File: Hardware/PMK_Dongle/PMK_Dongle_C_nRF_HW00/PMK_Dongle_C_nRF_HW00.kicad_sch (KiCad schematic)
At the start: 2 parts, among them J1 USB4151-GF-C, U1 NRF52840-CKAA-F-R7

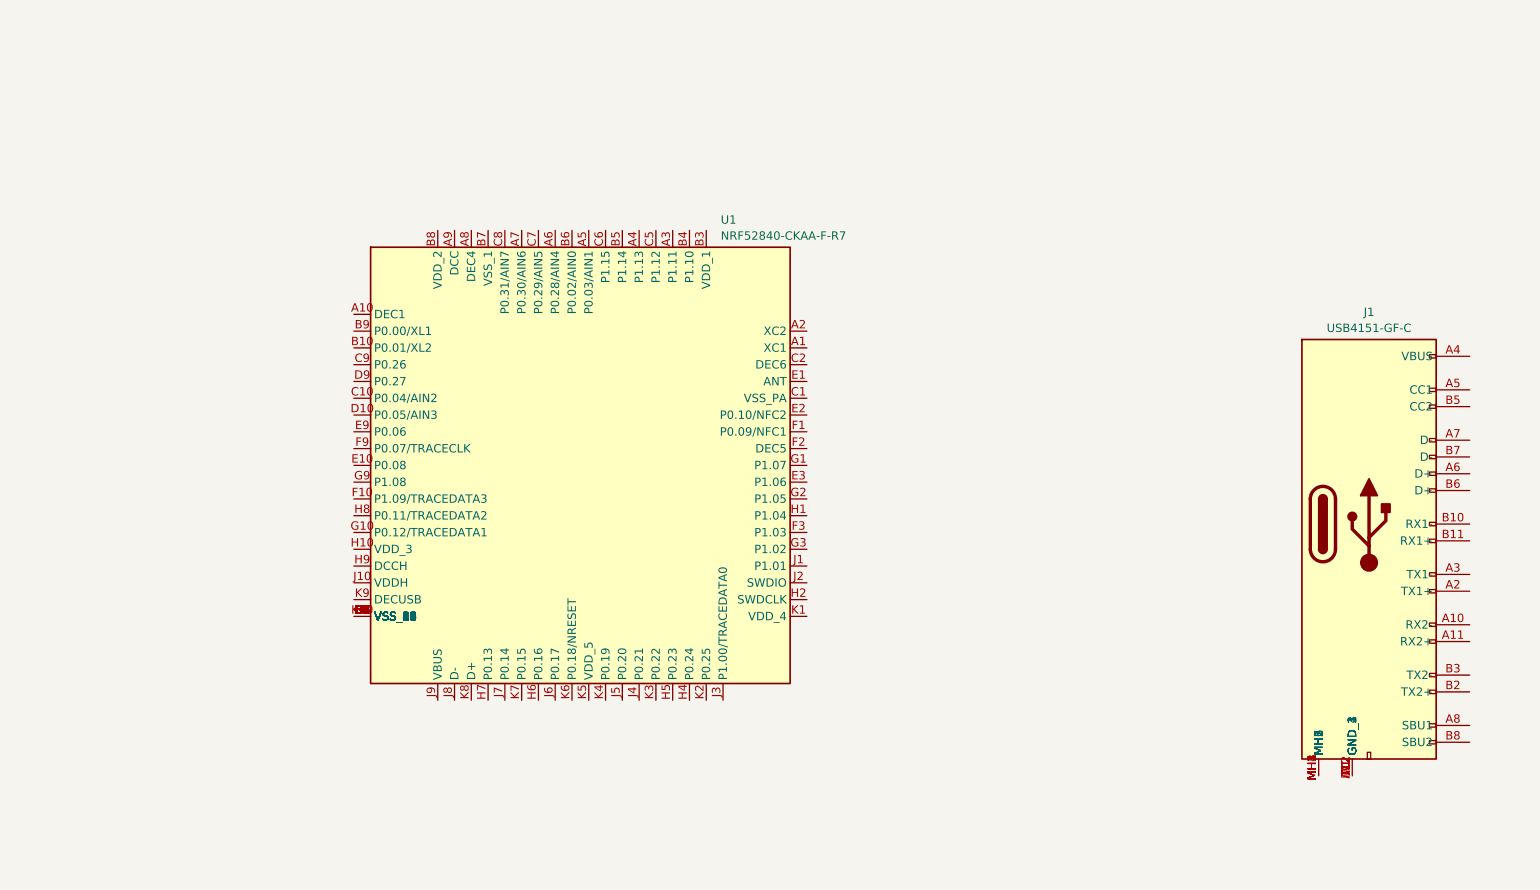
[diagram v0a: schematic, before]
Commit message: started routing PMK_Dongle_C_NRF_00
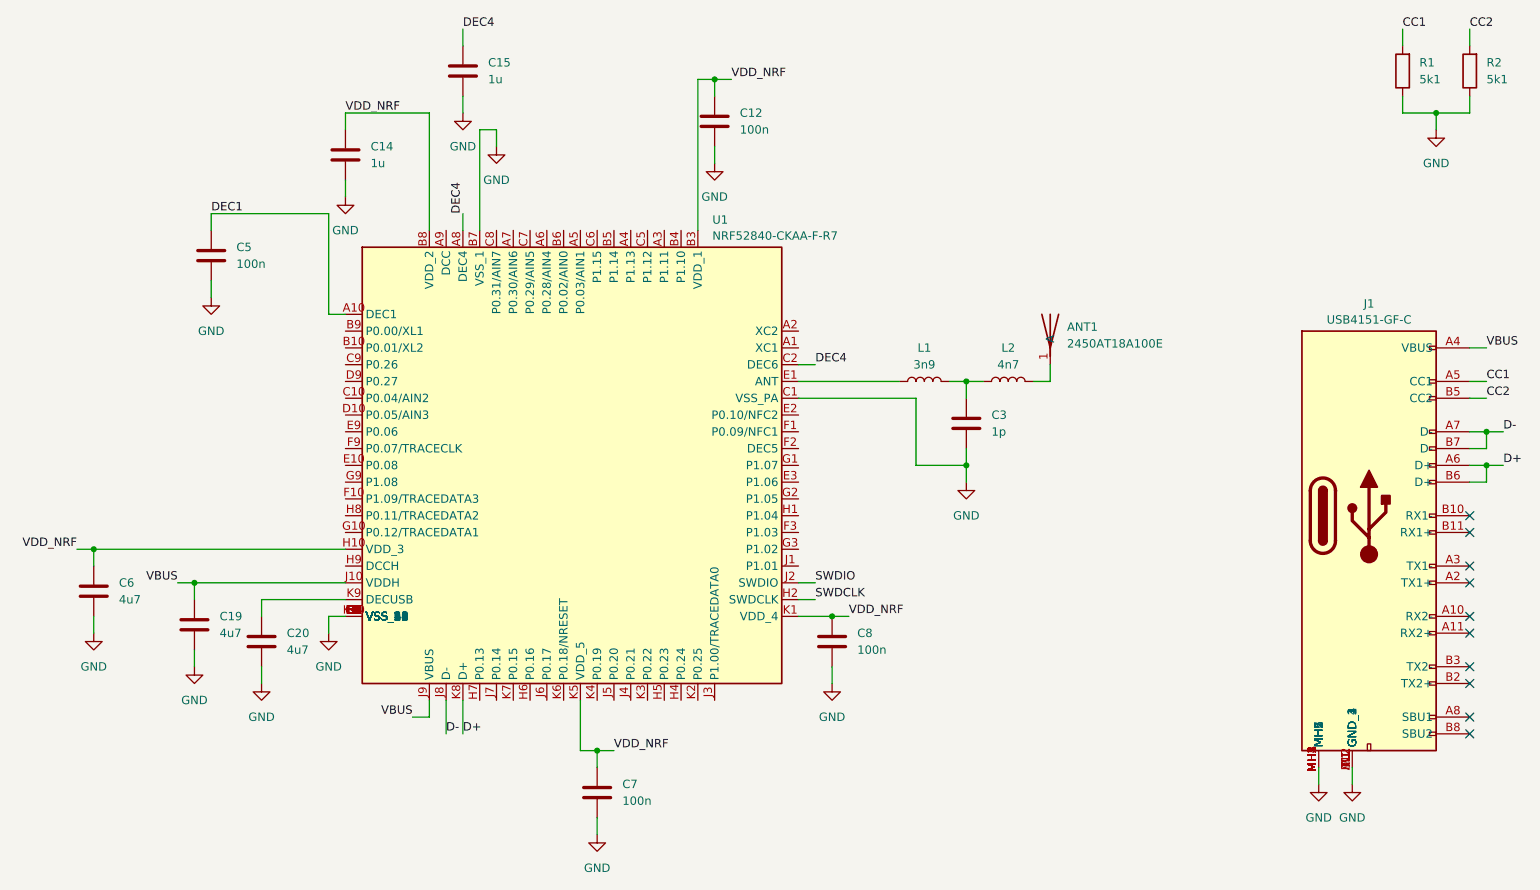
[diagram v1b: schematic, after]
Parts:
- added ANT1: 2450AT18A100E, Component_lib:ANTC3216X140N, symbol Component_lib:2450AT18A100E
- added C12, C5, C7, C8: 100n, Capacitor_SMD:C_0201_0603Metric, symbol Component_lib:C
- added C14, C15: 1u, Capacitor_SMD:C_0402_1005Metric, symbol Component_lib:C
- added C19, C20, C6: 4u7, Capacitor_SMD:C_0603_1608Metric, symbol Component_lib:C
- added C3: 1p, Capacitor_SMD:C_0201_0603Metric, symbol Component_lib:C
- added L1: 3n9, Inductor_SMD:L_0201_0603Metric, symbol Component_lib:L
- added L2: 4n7, Inductor_SMD:L_0201_0603Metric, symbol Component_lib:L
- added R1, R2: 5k1, Resistor_SMD:R_0201_0603Metric, symbol Component_lib:R
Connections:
- net DEC1: now reaches U1.A10 (DEC1)
- net DEC1: now also C5.1
- net DEC4: now reaches U1.A8 (DEC4)
- net DEC4: now also U1.C2 (DEC6), C15.1
- net VDD_NRF: now reaches U1.B3 (VDD_1)
- net VDD_NRF: now also U1.B8 (VDD_2), U1.H10 (VDD_3), U1.K1 (VDD_4), U1.K5 (VDD_5), C12.1, C14.1, C6.1, C7.1, C8.1
- net GND: now reaches U1.B7 (VSS_1)
- net GND: now also J1.A1 (GND_1), J1.A12 (GND_2), J1.B1 (GND_3), J1.B12 (GND_4), J1.MH1, J1.MH2 (MH7), J1.MH3 (MH2), J1.MH4 (MH6), J1.MH5, U1.C1 (VSS_PA), U1.C4 (VSS_2), U1.D3 (VSS_3), U1.D4 (VSS_4), U1.D5 (VSS_5), U1.D6 (VSS_6), U1.D7 (VSS_7), U1.D8 (VSS_8), U1.E4 (VSS_9), U1.E5 (VSS_10), U1.E6 (VSS_11), U1.E7 (VSS_12), U1.E8 (VSS_13), U1.F4 (VSS_14), U1.F5 (VSS_15), U1.F6 (VSS_16), U1.F7 (VSS_17), U1.F8 (VSS_18), U1.G4 (VSS_19), U1.G5 (VSS_20), U1.G6 (VSS_21), U1.G7 (VSS_22), U1.G8 (VSS_23), U1.K10 (VSS_24), C12.2, C14.2, C15.2, C19.2, C20.2, C3.2, C5.2, C6.2, C7.2, C8.2, R1.1, R2.1
- net at U1.E1 (ANT): now also L1.1
- net SWDCLK: now reaches U1.H2 (SWDCLK)
- net VBUS: now reaches U1.J10 (VDDH)
- net VBUS: now also J1.A4 (VBUS), J1.A9 (VBUS), J1.B4 (VBUS), J1.B9 (VBUS), U1.J9 (VBUS), C19.1
- net SWDIO: now reaches U1.J2 (SWDIO)
- net D-: now reaches U1.J8 (D-)
- net D-: now also J1.A7 (D-), J1.B7 (D-)
- net D+: now reaches U1.K8 (D+)
- net D+: now also J1.A6 (D+), J1.B6 (D+)
- net at U1.K9 (DECUSB): now also C20.1
- net CC1: now reaches J1.A5 (CC1)
- net CC1: now also R1.2
- net CC2: now reaches J1.B5 (CC2)
- net CC2: now also R2.2
- new net: C3.1, L1.2, L2.1
- new net: ANT1.1 (A), L2.2
- no-connect marks 0 -> 10
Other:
- moved on the sheet: J1, U1
